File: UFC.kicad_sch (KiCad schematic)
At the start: 48 parts, among them M1 Fan_3pin, M2 Fan_3pin, M3 Fan_3pin, M4 Fan_3pin, M5 Fan_3pin, M6 Fan_3pin, M7 Fan_3pin, M8 Fan_3pin, U1 Pico

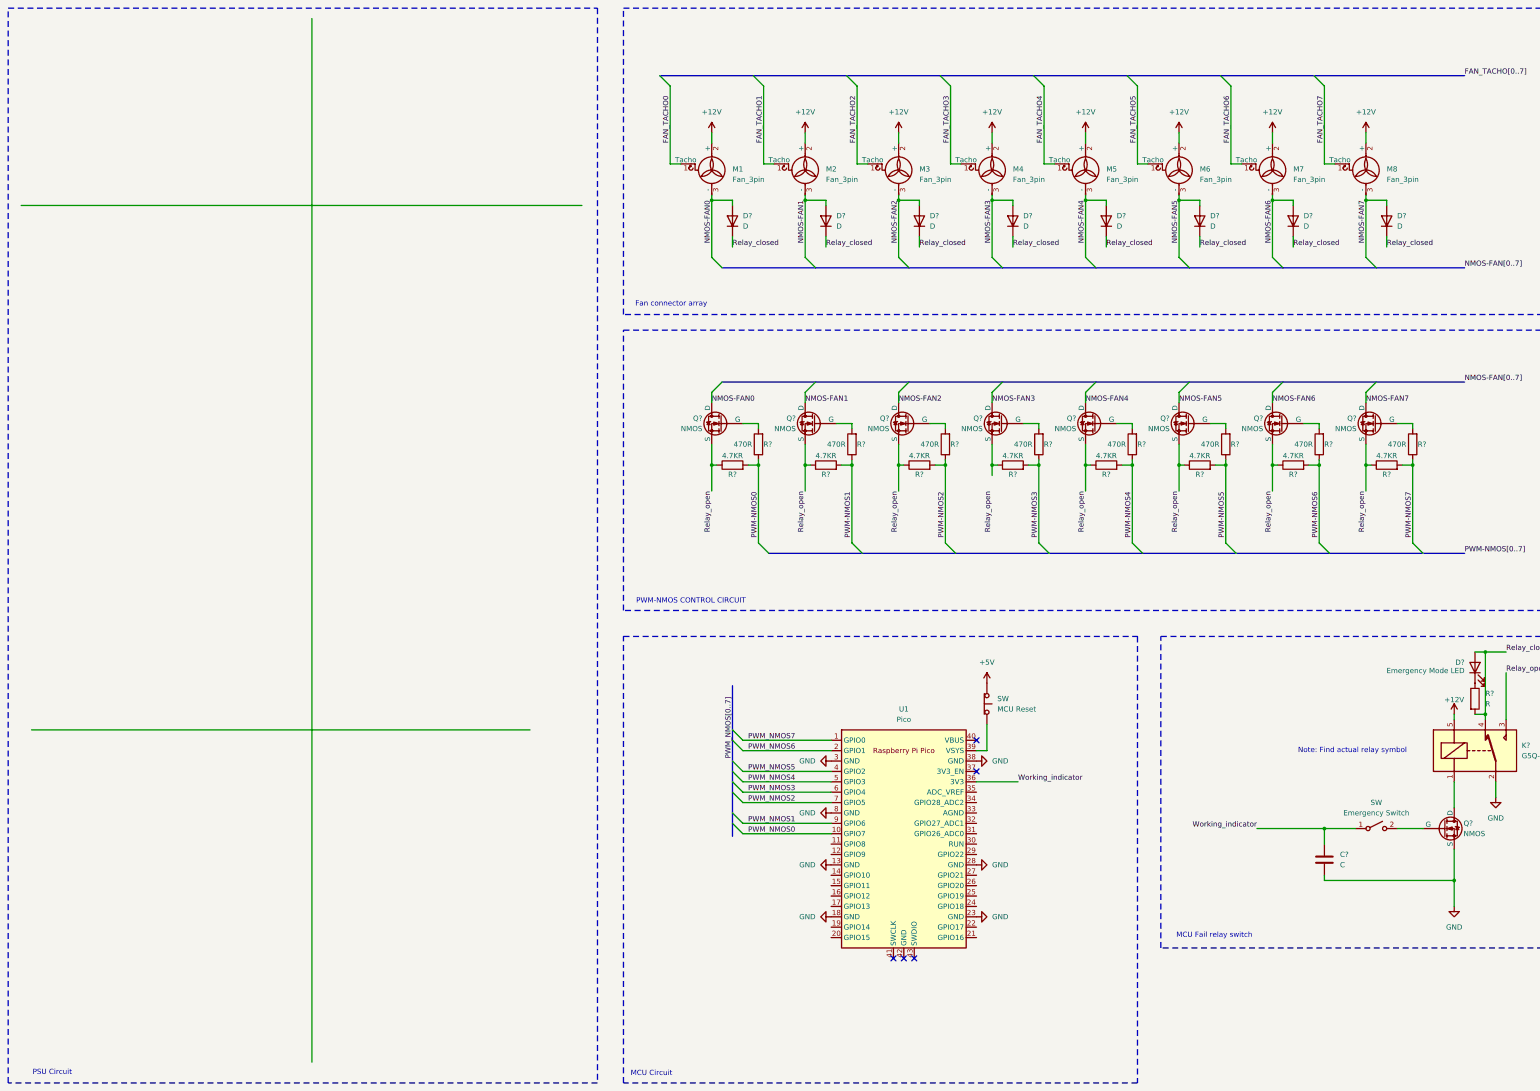
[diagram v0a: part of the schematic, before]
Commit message: Add safe relay discharge diode
Add safe relay discharge diode, clean up testing wires
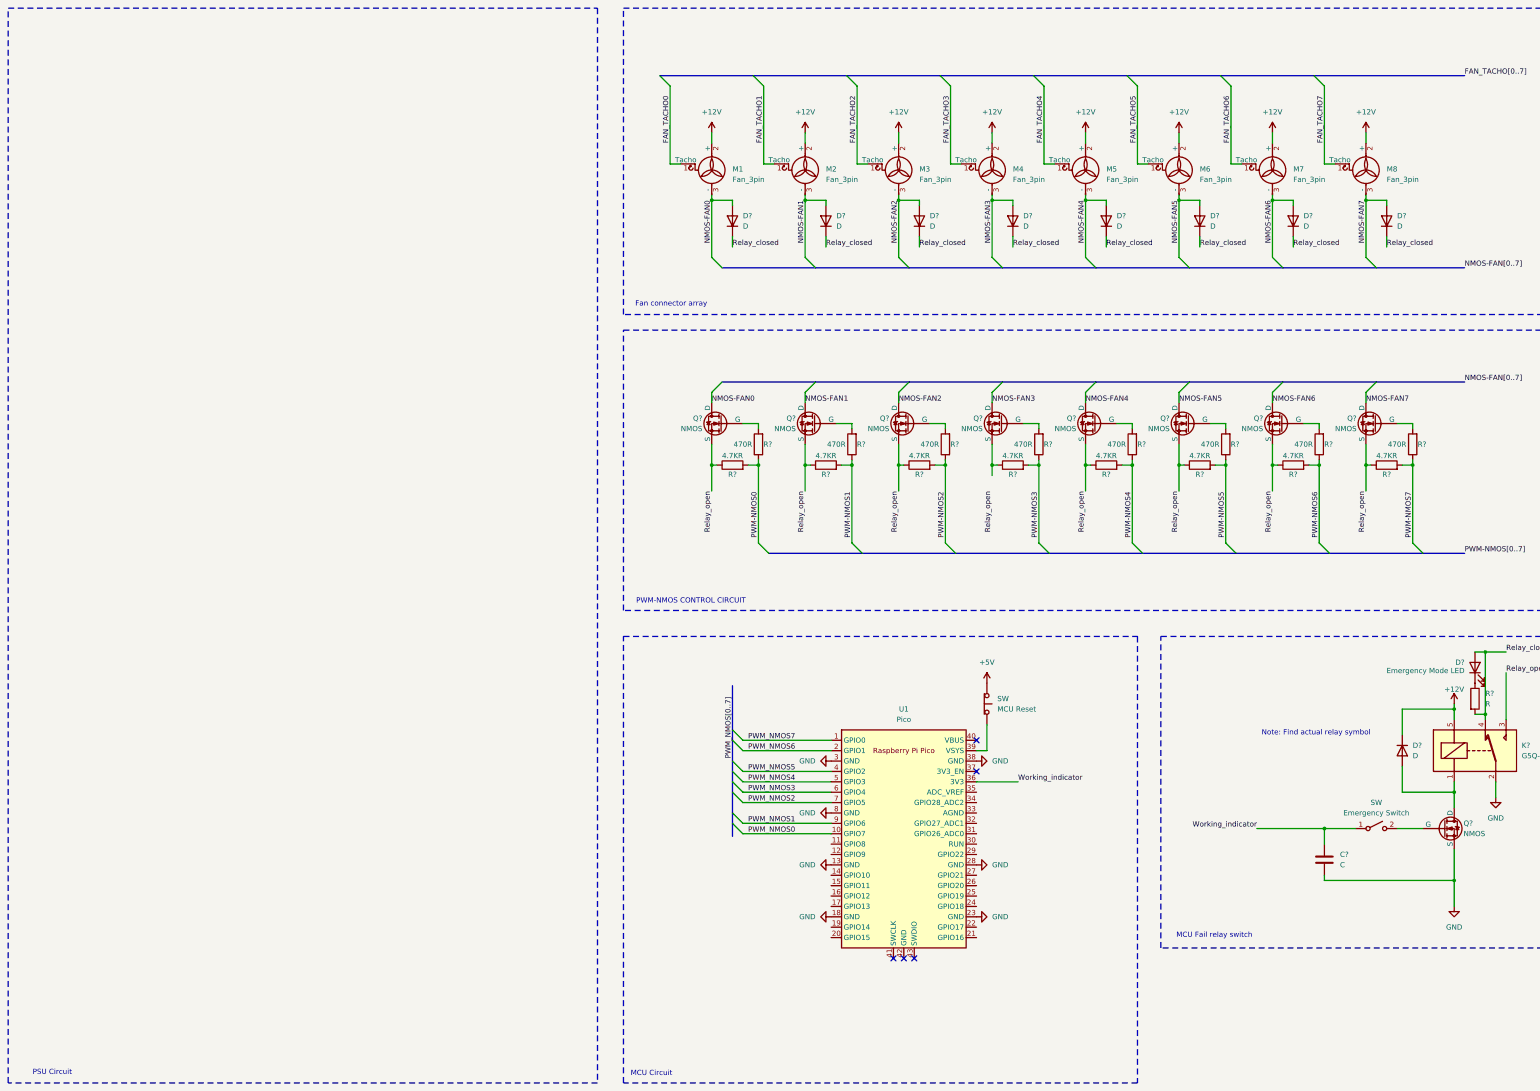
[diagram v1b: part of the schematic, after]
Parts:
- added D?: D, symbol Device:D
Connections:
- net +12V: now also D?.1 (K)
- net at K?.1, Q?.1 (D): now also D?.2 (A)
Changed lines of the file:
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@@
 	)
 	(junction
+		(at 372.11 189.23)
+		(diameter 0)
+		(color 0 0 0 0)
+	)
+	(junction
 		(at 190.5 64.77)
 		(diameter 0)
@@
 	)
 	(junction
+		(at 372.11 209.55)
+		(diameter 0)
+		(color 0 0 0 0)
+	)
+	(junction
 		(at 372.11 231.14)
 		(diameter 0)
@@
 	(wire
 		(pts
+			(xy 359.41 195.58) (xy 359.41 189.23)
+		)
+		(stroke
+			(width 0)
+			(type default)
+		)
+	)
+	(wire
+		(pts
 			(xy 248.92 55.88) (xy 251.46 55.88)
 		)
@@
 	(wire
 		(pts
-			(xy 21.59 66.04) (xy 158.75 66.04)
-		)
-		(stroke
-			(width 0)
-			(type default)
-		)
-	)
-	(wire
-		(pts
 			(xy 306.07 129.54) (xy 304.8 129.54)
 		)
@@
 	(wire
 		(pts
+			(xy 359.41 203.2) (xy 359.41 209.55)
+		)
+		(stroke
+			(width 0)
+			(type default)
+		)
+	)
+	(wire
+		(pts
 			(xy 361.95 129.54) (xy 361.95 148.59)
 		)
@@
 		)
 	)
+	(wire
+		(pts
+			(xy 359.41 189.23) (xy 372.11 189.23)
+		)
+		(stroke
+			(width 0)
+			(type default)
+		)
+	)
 	(bus
 		(pts
@@
 	(wire
 		(pts
-			(xy 372.11 190.5) (xy 372.11 191.77)
+			(xy 372.11 209.55) (xy 372.11 213.36)
 		)
 		(stroke
@@
 	(wire
 		(pts
-			(xy 24.13 194.31) (xy 146.05 194.31)
+			(xy 372.11 187.96) (xy 372.11 189.23)
 		)
 		(stroke
@@
 	(wire
 		(pts
-			(xy 92.71 20.32) (xy 92.71 275.59)
-		)
-		(stroke
-			(width 0)
-			(type default)
-		)
-	)
-	(wire
-		(pts
 			(xy 382.27 207.01) (xy 382.27 210.82)
 		)
@@
 	(wire
 		(pts
-			(xy 372.11 207.01) (xy 372.11 213.36)
+			(xy 372.11 207.01) (xy 372.11 209.55)
 		)
 		(stroke
@@
 	(wire
 		(pts
+			(xy 372.11 189.23) (xy 372.11 191.77)
+		)
+		(stroke
+			(width 0)
+			(type default)
+		)
+	)
+	(wire
+		(pts
 			(xy 257.81 193.04) (xy 257.81 199.39)
 		)
@@
 		)
 	)
+	(wire
+		(pts
+			(xy 359.41 209.55) (xy 372.11 209.55)
+		)
+		(stroke
+			(width 0)
+			(type default)
+		)
+	)
 	(bus
 		(pts
@@
 	(text "Note: Find actual relay symbol"
 		(exclude_from_sim no)
-		(at 347.218 199.39 0)
+		(at 338.328 195.072 0)
 		(effects
 			(font
@@
 	)
 	(symbol
+		(lib_id "Device:D")
+		(at 359.41 199.39 270)
+		(unit 1)
+		(exclude_from_sim no)
+		(in_bom yes)
+		(on_board yes)
+		(dnp no)
+		(fields_autoplaced yes)
+		(property "Reference" "D?"
+			(at 361.95 198.1199 90)
+			(effects
+				(font
+					(size 1.27 1.27)
+				)
+				(justify left)
+			)
+		)
+		(property "Value" "D"
+			(at 361.95 200.6599 90)
+			(effects
+				(font
+					(size 1.27 1.27)
+				)
+				(justify left)
+			)
+		)
+		(property "Footprint" ""
+			(at 359.41 199.39 0)
+			(effects
+				(font
+					(size 1.27 1.27)
+				)
+				(hide yes)
+			)
+		)
+		(property "Datasheet" "~"
+			(at 359.41 199.39 0)
+			(effects
+				(font
+					(size 1.27 1.27)
+				)
+				(hide yes)
+			)
+		)
+		(property "Description" "Diode"
+			(at 359.41 199.39 0)
+			(effects
+				(font
+					(size 1.27 1.27)
+				)
+				(hide yes)
+			)
+		)
+		(property "Sim.Device" "D"
+			(at 359.41 199.39 0)
+			(effects
+				(font
+					(size 1.27 1.27)
+				)
+				(hide yes)
+			)
+		)
+		(property "Sim.Pins" "1=K 2=A"
+			(at 359.41 199.39 0)
+			(effects
+				(font
+					(size 1.27 1.27)
+				)
+				(hide yes)
+			)
+		)
+		(pin "2"
+		)
+		(pin "1"
+		)
+		(instances
+			(project "UFC"
+				(path "/342a3fd1-b517-460b-a70f-feeb7547ac4b"
+					(reference "D?")
+					(unit 1)
+				)
+			)
+		)
+	)
+	(symbol
 		(lib_id "Simulation_SPICE:NMOS")
 		(at 307.34 119.38 0)
@@
 	(symbol
 		(lib_id "power:+12V")
-		(at 372.11 190.5 0)
+		(at 372.11 187.96 0)
 		(unit 1)
 		(exclude_from_sim no)
@@
 		(dnp no)
 		(property "Reference" "#PWR020"
-			(at 372.11 194.31 0)
+			(at 372.11 191.77 0)
 			(effects
 				(font
@@
 		)
 		(property "Value" "+12V"
-			(at 372.11 186.944 0)
+			(at 372.11 184.404 0)
 			(effects
 				(font
@@
 		)
 		(property "Footprint" ""
-			(at 372.11 190.5 0)
+			(at 372.11 187.96 0)
 			(effects
 				(font
@@
 		)
 		(property "Datasheet" ""
-			(at 372.11 190.5 0)
+			(at 372.11 187.96 0)
 			(effects
 				(font
@@
 		)
 		(property "Description" "Power symbol creates a global label with name \"+12V\""
-			(at 372.11 190.5 0)
+			(at 372.11 187.96 0)
 			(effects
 				(font

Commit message: Tweak relay circuit
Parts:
- removed C?: C, symbol Device:C
- added R? (x2): R, symbol Device:R
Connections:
- net GND: now also SW.2 (B), R?.2; no longer Q?.3 (S)
- net Working_indicator: now also R?.1, R?.2; no longer SW.1 (A)
- net at Q?.2 (G): now also R?.1; no longer SW.2 (B)
- new net: Q?.3 (S), SW.1 (A)
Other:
- moved on the sheet: SW

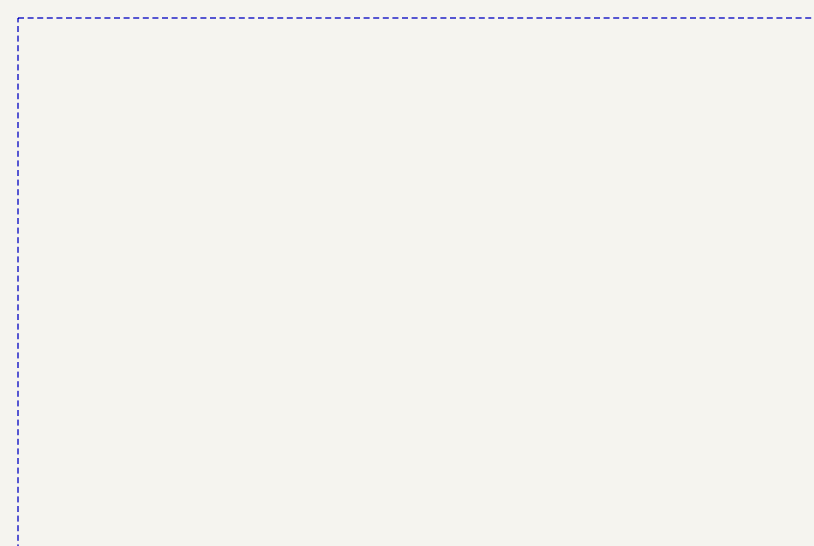
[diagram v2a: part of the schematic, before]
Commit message: Update UFC.kicad_sch
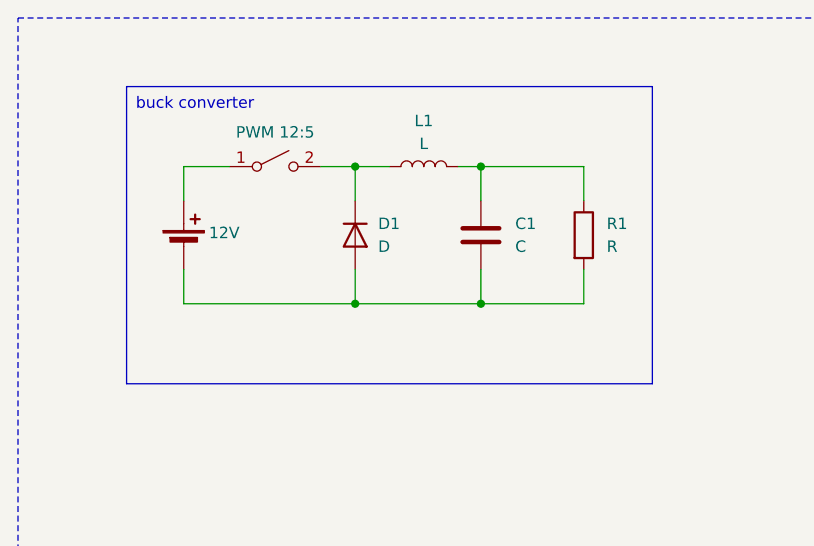
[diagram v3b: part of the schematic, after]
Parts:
- added BT1: 12V, symbol Device:Battery_Cell
- added C1: C, symbol Device:C
- added D1: D, symbol Device:D
- added L1: L, symbol Device:L
- added R1: R, symbol Device:R
- added SW1: PWM 12:5, symbol Switch:SW_SPST
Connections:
- new net: D1.1 (K), L1.1, SW1.2 (B)
- new net: C1.1, L1.2, R1.1
- new net: BT1.2 (-), C1.2, D1.2 (A), R1.2
- new net: BT1.1 (+), SW1.1 (A)
